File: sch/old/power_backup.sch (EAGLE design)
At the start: 34 parts, among them IC1 78L05SMD, IC2 ACS712-LC, K1 DS2Y-S-DC48V, T1 BC847, T2 BC847, T3 BC847

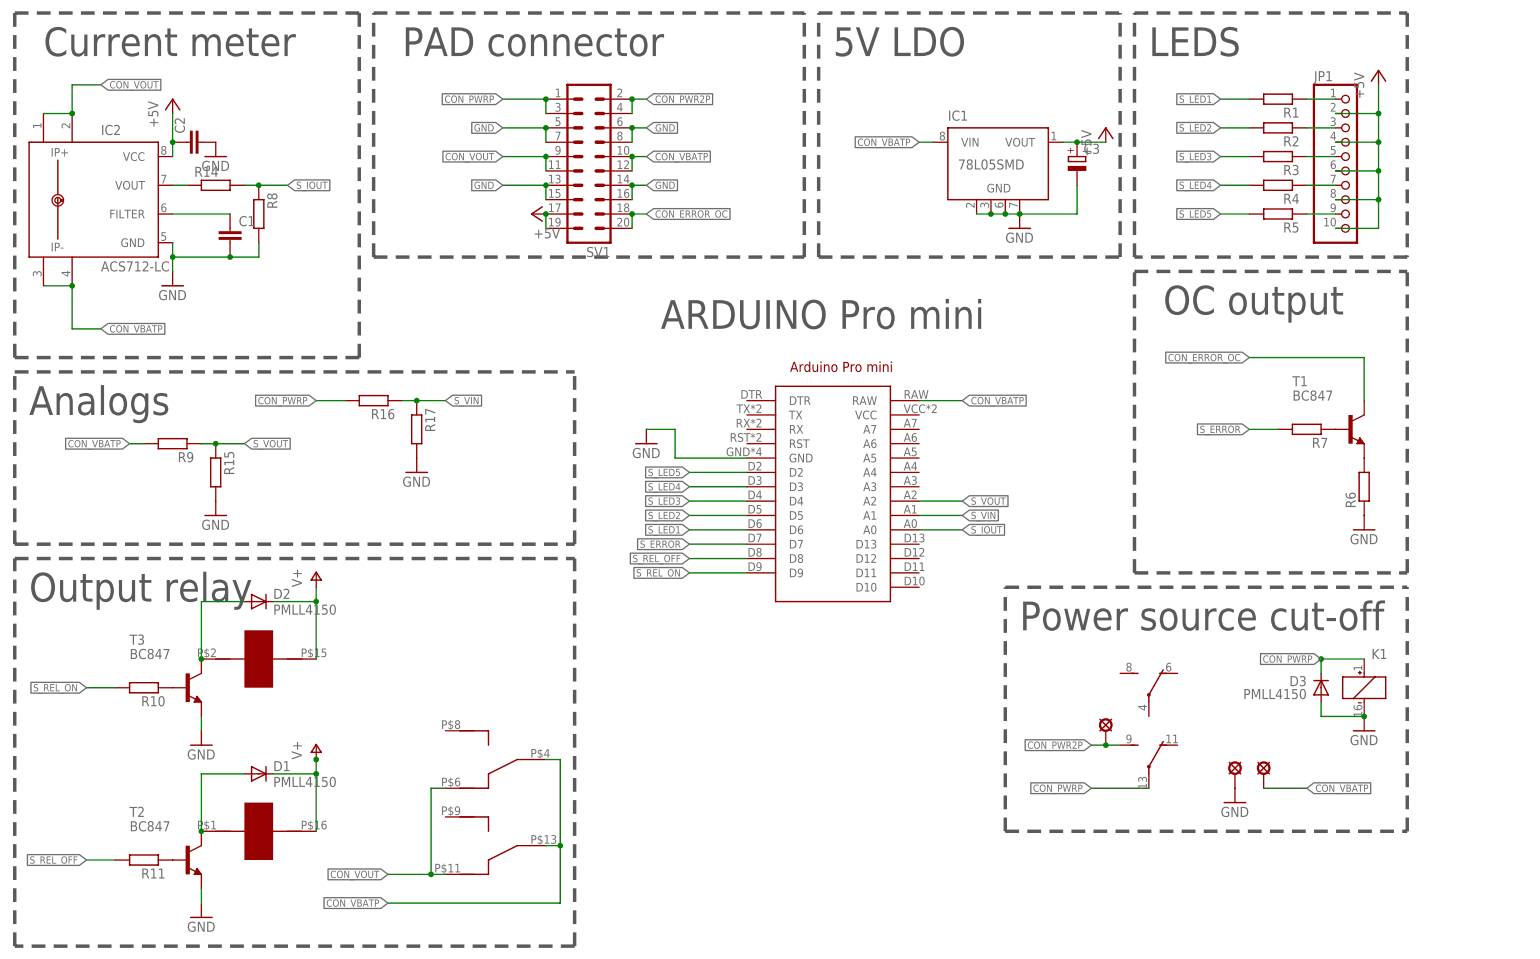
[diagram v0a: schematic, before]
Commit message: code example added
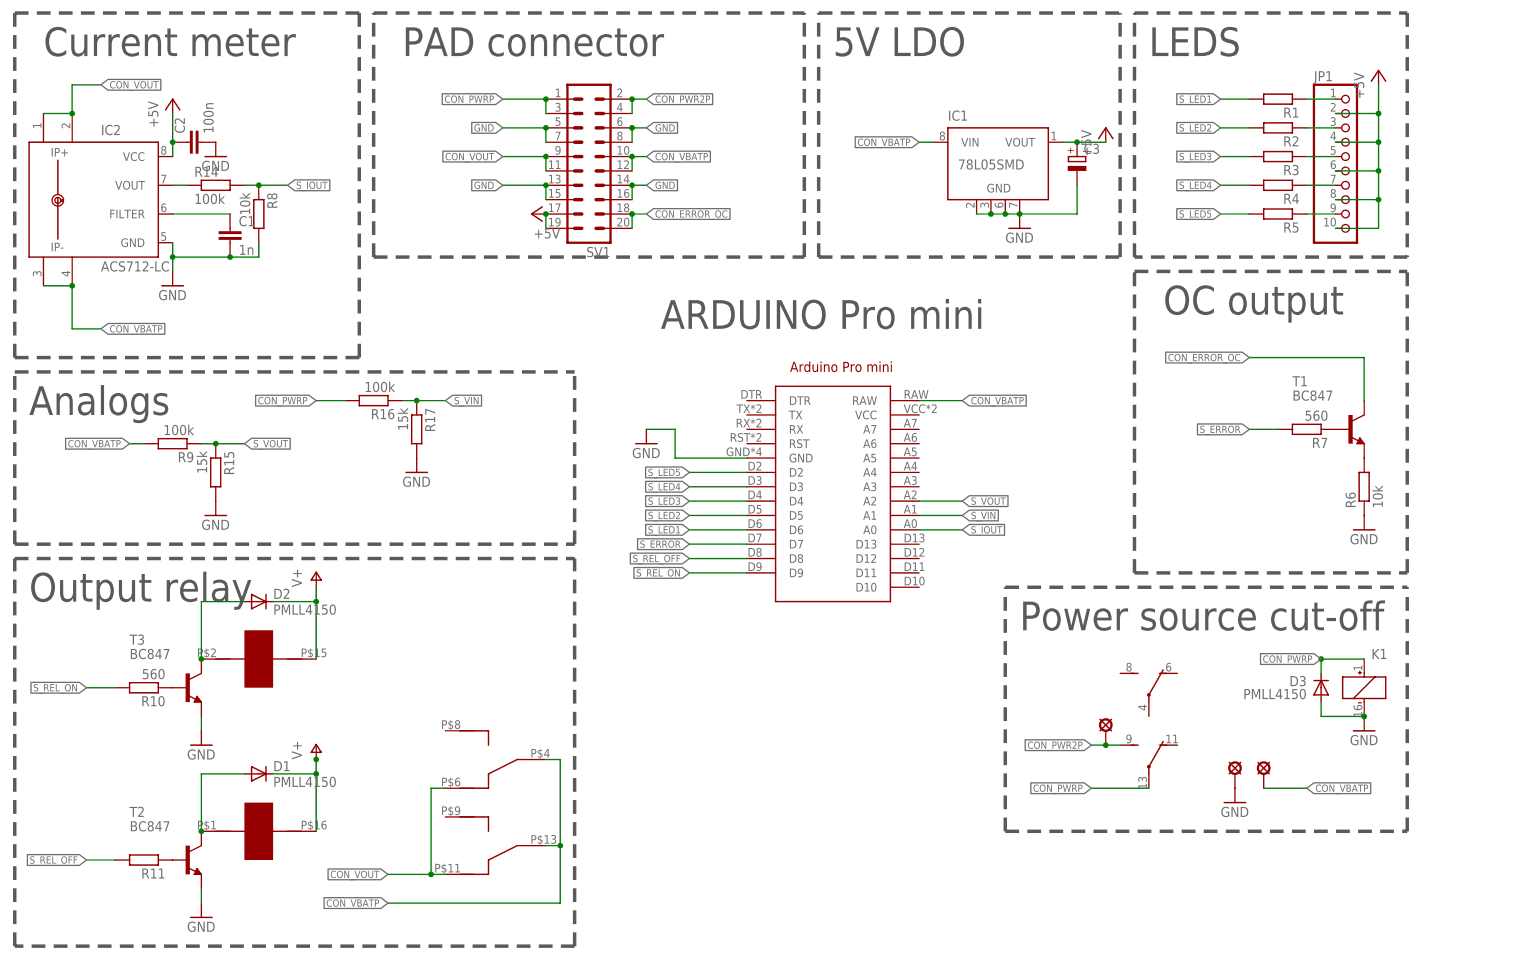
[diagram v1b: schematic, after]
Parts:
- C1: value (none) -> 1n
- C2: value (none) -> 100n
- R10, R7: value (none) -> 560
- R14, R16, R9: value (none) -> 100k
- R15, R17: value (none) -> 15k
- R6, R8: value (none) -> 10k
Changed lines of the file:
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@@
 <part name="R4" library="rcl" deviceset="R-EU_" device="M0805"/>
 <part name="R5" library="rcl" deviceset="R-EU_" device="M0805"/>
-<part name="R6" library="rcl" deviceset="R-EU_" device="M0805"/>
+<part name="R6" library="rcl" deviceset="R-EU_" device="M0805" value="10k"/>
 <part name="GND1" library="supply1" deviceset="GND" device=""/>
-<part name="R7" library="rcl" deviceset="R-EU_" device="M0805"/>
+<part name="R7" library="rcl" deviceset="R-EU_" device="M0805" value="560"/>
 <part name="GND2" library="supply1" deviceset="GND" device=""/>
-<part name="R8" library="rcl" deviceset="R-EU_" device="M0805"/>
-<part name="R9" library="rcl" deviceset="R-EU_" device="M0805"/>
+<part name="R8" library="rcl" deviceset="R-EU_" device="M0805" value="10k"/>
+<part name="R9" library="rcl" deviceset="R-EU_" device="M0805" value="100k"/>
 <part name="U$1" library="relay_hfd2" deviceset="HFD2/003" device=""/>
 <part name="T2" library="transistor" deviceset="BC847" device=""/>
 <part name="T3" library="transistor" deviceset="BC847" device=""/>
-<part name="R10" library="rcl" deviceset="R-EU_" device="M0805"/>
+<part name="R10" library="rcl" deviceset="R-EU_" device="M0805" value="560"/>
 <part name="R11" library="rcl" deviceset="R-EU_" device="M0805"/>
 <part name="GND4" library="supply1" deviceset="GND" device=""/>
@@
 <part name="P+3" library="supply1" deviceset="V+" device=""/>
 <part name="IC2" library="allegro-2" deviceset="ACS712-LC" device=""/>
-<part name="R14" library="rcl" deviceset="R-EU_" device="M0805"/>
-<part name="R15" library="rcl" deviceset="R-EU_" device="M0805"/>
+<part name="R14" library="rcl" deviceset="R-EU_" device="M0805" value="100k"/>
+<part name="R15" library="rcl" deviceset="R-EU_" device="M0805" value="15k"/>
 <part name="GND7" library="supply1" deviceset="GND" device=""/>
-<part name="C1" library="rcl" deviceset="C-EU" device="C0805"/>
-<part name="C2" library="rcl" deviceset="C-EU" device="C0805"/>
+<part name="C1" library="rcl" deviceset="C-EU" device="C0805" value="1n"/>
+<part name="C2" library="rcl" deviceset="C-EU" device="C0805" value="100n"/>
 <part name="GND6" library="supply1" deviceset="GND" device=""/>
-<part name="R16" library="rcl" deviceset="R-EU_" device="M0805"/>
-<part name="R17" library="rcl" deviceset="R-EU_" device="M0805"/>
+<part name="R16" library="rcl" deviceset="R-EU_" device="M0805" value="100k"/>
+<part name="R17" library="rcl" deviceset="R-EU_" device="M0805" value="15k"/>
 <part name="GND3" library="supply1" deviceset="GND" device=""/>
 <part name="GND8" library="supply1" deviceset="GND" device=""/>
